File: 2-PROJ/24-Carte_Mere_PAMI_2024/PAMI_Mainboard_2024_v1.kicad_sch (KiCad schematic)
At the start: 20 parts, among them J1 Conn_01x08, J2 Conn_01x03, J3 USB_A, J4 Conn_01x03, J5 Conn_01x02, J6 Conn_01x04, J7 Conn_01x03, SW1 SW_DIP_x04, SW2 SW_DPST_x2

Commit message: Carte Mère PAMI - Work In Progress
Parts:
- added J24: Conn_01x06, Connector_PinSocket_2.54mm:PinSocket_1x06_P2.54mm_Vertical, symbol Connector_Generic:Conn_01x06
- added J25: Conn_02x05_Odd_Even, ConnectorsEvo:690357281076, symbol Connector_Generic:Conn_02x05_Odd_Even
- SW2: footprint (none) -> Connector_PinHeader_2.54mm:PinHeader_1x03_P2.54mm_Vertical
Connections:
- net +3.3VP: now also J24.3 (Pin_3)
- net +5V: now also J7.2 (Pin_2), J24.1 (Pin_1), J25.1 (Pin_1); no longer J7.1 (Pin_1)
- net CAN/CANH: now also J25.9 (Pin_9)
- net CAN/CANL: now also J25.10 (Pin_10)
- net CaptTOR_1: now also RP1.26 (GPIO7/SPI0_CE1)
- net CaptTOR_2: now also RP1.29 (GPIO5/GPCLK1)
- net GND: now also J7.1 (Pin_1), J24.2 (Pin_2), J24.6 (Pin_6), J25.3 (Pin_3), J25.4 (Pin_4); no longer J7.2 (Pin_2)
- net SIDE: now also RP1.18 (GPIO24)
- net at R9.1: now also RP1.7 (GPIO4/GPCLK0), SW1.4; no longer SW1.1
- net at R11.1: now also RP1.16 (GPIO23), SW1.2; no longer SW1.3
- net +5V_IN: now reaches J1.8 (Pin_8), SW2.2 (B)
- net at R10.1: now also RP1.13 (GPIO27), SW1.3; no longer SW1.2
- net at R12.1: now also RP1.15 (GPIO22), SW1.1; no longer SW1.4
- net at RP1.10 (GPIO15/UART_RX): now also J24.4 (Pin_4)
- net at RP1.8 (GPIO14/UART_TX): now also J24.5 (Pin_5)
- net CAN/INT renamed INT_CAN
- net SX1509/INT renamed INT_SX
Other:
- note added: "JeVois A33 alim & UART"
- note added: "Movement Tracker"
- moved on the sheet: J5, J7

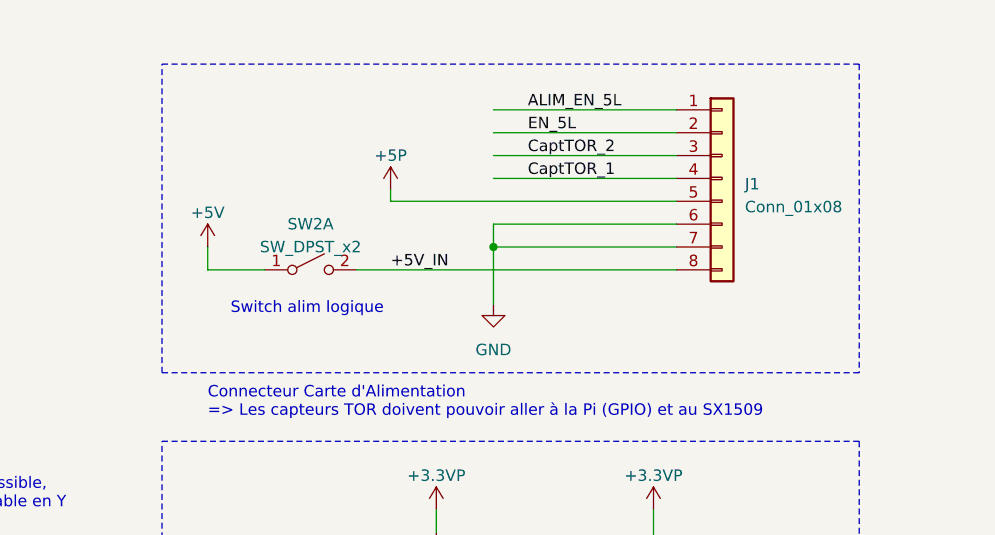
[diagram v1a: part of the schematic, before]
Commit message: CM PAMI 2024 - Correction interrupteur 5V
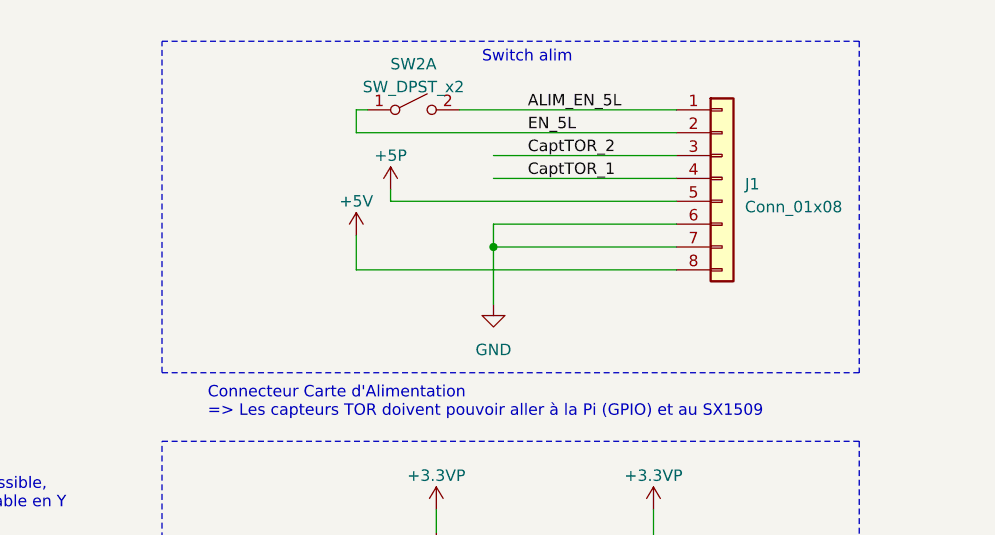
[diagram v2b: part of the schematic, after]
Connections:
- net +5V: now also J1.8 (Pin_8); no longer SW2.1 (A)
- net ALIM_EN_5L: now also SW2.2 (B)
- net EN_5L: now also SW2.1 (A)
- removed net +5V_IN: J1.8 (Pin_8), SW2.2 (B)
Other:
- note added: "Switch alim"
- note removed: "Switch alim logique"
- moved on the sheet: SW2A
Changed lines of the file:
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@@
+    (stroke (width 0) (type default))
+  )
+  (wire (pts (xy 220.98 24.13) (xy 219.71 24.13))
     (stroke (width 0) (type default))
   )
@@
     (stroke (width 0) (type default))
   )
-  (wire (pts (xy 234.95 24.13) (xy 255.27 24.13))
+  (wire (pts (xy 231.14 24.13) (xy 255.27 24.13))
     (stroke (width 0) (type default))
   )
@@
     (stroke (width 0) (type default))
   )
+  (wire (pts (xy 219.71 38.1) (xy 219.71 41.91))
+    (stroke (width 0) (type default))
+  )
   (wire (pts (xy 67.31 86.36) (xy 160.02 86.36))
     (stroke (width 0) (type default))
@@
     (stroke (width 0) (type default))
   )
-  (wire (pts (xy 209.55 41.91) (xy 203.2 41.91))
-    (stroke (width 0) (type default))
-  )
   (wire (pts (xy 67.31 53.34) (xy 71.12 53.34))
     (stroke (width 0) (type default))
@@
     (stroke (width 0) (type default))
   )
-  (wire (pts (xy 203.2 41.91) (xy 203.2 39.37))
-    (stroke (width 0) (type default))
-  )
   (wire (pts (xy 267.97 133.35) (xy 267.97 135.89))
     (stroke (width 0) (type default))
@@
     (stroke (width 0) (type default))
   )
+  (wire (pts (xy 255.27 41.91) (xy 219.71 41.91))
+    (stroke (width 0) (type default))
+  )
   (wire (pts (xy 83.82 38.1) (xy 82.55 38.1))
     (stroke (width 0) (type default))
@@
     (stroke (width 0) (type default))
   )
-  (wire (pts (xy 234.95 26.67) (xy 255.27 26.67))
+  (wire (pts (xy 219.71 26.67) (xy 255.27 26.67))
     (stroke (width 0) (type default))
   )
@@
     (stroke (width 0) (type default))
   )
+  (wire (pts (xy 219.71 24.13) (xy 219.71 26.67))
+    (stroke (width 0) (type default))
+  )
   (wire (pts (xy 68.58 162.56) (xy 68.58 165.1))
     (stroke (width 0) (type default))
@@
   )
   (wire (pts (xy 67.31 74.93) (xy 86.36 74.93))
-    (stroke (width 0) (type default))
-  )
-  (wire (pts (xy 255.27 41.91) (xy 219.71 41.91))
     (stroke (width 0) (type default))
   )
@@
     (fill (type none))
   )
-  (rectangle (start 198.12 19.05) (end 275.59 53.34)
+  (rectangle (start 198.12 16.51) (end 275.59 53.34)
     (stroke (width 0) (type dash))
     (fill (type none))
@@
     (effects (font (size 1.27 1.27)) (justify left bottom))
   )
-  (text "Switch alim logique" (at 205.74 46.99 0)
+  (text "Switch alim" (at 233.68 19.05 0)
     (effects (font (size 1.27 1.27)) (justify left bottom))
   )
@@
   )
   (label "SIDE" (at 208.28 151.13 0) (fields_autoplaced)
-    (effects (font (size 1.27 1.27)) (justify left bottom))
-  )
-  (label "+5V_IN" (at 223.52 41.91 0) (fields_autoplaced)
     (effects (font (size 1.27 1.27)) (justify left bottom))
   )
@@
     )
   )
-  (symbol (lib_id "Switch:SW_DPST_x2") (at 214.63 41.91 0) (unit 1)
-    (in_bom yes) (on_board yes) (dnp no) (fields_autoplaced)
-    (property "Reference" "SW2" (at 214.63 36.83 0)
-      (effects (font (size 1.27 1.27)))
-    )
-    (property "Value" "SW_DPST_x2" (at 214.63 39.37 0)
-      (effects (font (size 1.27 1.27)))
-    )
-    (property "Footprint" "Connector_PinHeader_2.54mm:PinHeader_1x03_P2.54mm_Vertical" (at 214.63 41.91 0)
-      (effects (font (size 1.27 1.27)) hide)
-    )
-    (property "Datasheet" "~" (at 214.63 41.91 0)
+  (symbol (lib_id "Switch:SW_DPST_x2") (at 226.06 24.13 0) (unit 1)
+    (in_bom yes) (on_board yes) (dnp no) (fields_autoplaced)
+    (property "Reference" "SW2" (at 226.06 19.05 0)
+      (effects (font (size 1.27 1.27)))
+    )
+    (property "Value" "SW_DPST_x2" (at 226.06 21.59 0)
+      (effects (font (size 1.27 1.27)))
+    )
+    (property "Footprint" "Connector_PinHeader_2.54mm:PinHeader_1x03_P2.54mm_Vertical" (at 226.06 24.13 0)
+      (effects (font (size 1.27 1.27)) hide)
+    )
+    (property "Datasheet" "~" (at 226.06 24.13 0)
       (effects (font (size 1.27 1.27)) hide)
     )
@@
     )
   )
-  (symbol (lib_id "power:+5V") (at 203.2 39.37 0) (unit 1)
-    (in_bom yes) (on_board yes) (dnp no) (fields_autoplaced)
-    (property "Reference" "#PWR021" (at 203.2 43.18 0)
-      (effects (font (size 1.27 1.27)) hide)
-    )
-    (property "Value" "+5V" (at 203.2 35.56 0)
-      (effects (font (size 1.27 1.27)))
-    )
-    (property "Footprint" "" (at 203.2 39.37 0)
-      (effects (font (size 1.27 1.27)) hide)
-    )
-    (property "Datasheet" "" (at 203.2 39.37 0)
-      (effects (font (size 1.27 1.27)) hide)
-    )
+  (symbol (lib_id "power:+5V") (at 219.71 38.1 0) (unit 1)
+    (in_bom yes) (on_board yes) (dnp no) (fields_autoplaced)
+    (property "Reference" "#PWR021" (at 219.71 41.91 0)
+      (effects (font (size 1.27 1.27)) hide)
+    )
+    (property "Value" "+5V" (at 219.71 34.29 0)
+      (effects (font (size 1.27 1.27)))
+    )
+    (property "Footprint" "" (at 219.71 38.1 0)
+      (effects (font (size 1.27 1.27)) hide)
+    )
+    (property "Datasheet" "" (at 219.71 38.1 0)
+      (effects (font (size 1.27 1.27)) hide)
+    )

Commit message: CM PAMI 2024 - WIP
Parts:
- added C11: 100nF, Capacitor_SMD:C_0603_1608Metric, symbol Device:C
- added C8: 470uF, Capacitor_THT:C_Radial_D8.0mm_H11.5mm_P3.50mm, symbol Device:C_Polarized_Small
- added D1: LED, LED_SMD:LED_0603_1608Metric, symbol Device:LED
- added H1, H2, H3, H4: MountingHole_Pad, MountingHole:MountingHole_3.2mm_M3_Pad_Via, symbol Mechanical:MountingHole_Pad
- added R16, R17, R18, R19, R22: 10K, Resistor_SMD:R_0603_1608Metric_Pad0.98x0.95mm_HandSolder, symbol Device:R
- added R20: 68, Resistor_SMD:R_0603_1608Metric_Pad0.98x0.95mm_HandSolder, symbol Device:R
- added R21: R, Resistor_SMD:R_0603_1608Metric, symbol Device:R
- added R23, R24, R25, R26: 1K, Resistor_SMD:R_0603_1608Metric_Pad0.98x0.95mm_HandSolder, symbol Device:R
- R13: value 68 -> 1K
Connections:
- net +3.3VP: now also C11.1, R22.2; no longer J4.1 (Pin_1), RP1.1 (3V3)
- net +5P: now also D1.2 (A)
- net +5V: now also C8.1
- net CaptTOR_1: now also R18.2
- net CaptTOR_2: now also R16.2
- net GND: now also C11.2, C8.2, H1.1, H2.1, H3.1, H4.1, R17.1, R19.1, R21.1
- net WS2812B: now also R20.2; no longer J7.3 (Pin_3)
- net at R9.1, SW1.4: now also R26.1; no longer RP1.7 (GPIO4/GPCLK0)
- net at R11.1, SW1.2: now also R24.1; no longer RP1.16 (GPIO23)
- net at R12.1, SW1.1: now also R23.1; no longer RP1.15 (GPIO22)
- net at R10.1, SW1.3: now also R25.1; no longer RP1.13 (GPIO27)
- net at J4.2 (Pin_2), R13.1: now also R22.1
- new net: R16.1, R17.2
- new net: R23.2, RP1.15 (GPIO22)
- new net: J7.3 (Pin_3), R20.1
- new net: R18.1, R19.2
- new net: D1.1 (K), R21.2
- new net: R25.2, RP1.13 (GPIO27)
- new net: R26.2, RP1.7 (GPIO4/GPCLK0)
- new net: R24.2, RP1.16 (GPIO23)
- no-connect marks 0 -> 1
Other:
- note added: "Raccorder I2C du movement tracker"
- note added: "Raccorder le reset du tracker à une GPIO de la Pi Rajouter un bouton de "reset sauf Raspi""
- note added: "Trouver modele 3D pour le switch"
- note removed: "Vers 5 GPIO Raspi"
- moved on the sheet: C14, C15, J2, J24, R13, R7, R8

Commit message: CM PAMI 2024 - WIP
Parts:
- added D2, D3, D4: WS2812B, LED_SMD:LED_WS2812B_PLCC4_5.0x5.0mm_P3.2mm, symbol LED:WS2812B
- R21: value R -> 1K
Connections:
- net +5V: now also D2.1 (VDD), D3.1 (VDD), D4.1 (VDD)
- net GND: now also D2.3 (VSS), D3.3 (VSS), D4.3 (VSS)
- net at J7.3 (Pin_3): now also D4.2 (DOUT); no longer R20.1
- new net: D3.2 (DOUT), D4.4 (DIN)
- new net: D2.2 (DOUT), D3.4 (DIN)
- new net: D2.4 (DIN), R20.1
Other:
- moved on the sheet: J7

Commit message: fin routage carte Mere PAMI
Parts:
- added R43: 68, Resistor_SMD:R_0603_1608Metric_Pad0.98x0.95mm_HandSolder, symbol Device:R
- J24: footprint Connector_PinSocket_2.54mm:PinSocket_1x06_P2.54mm_Vertical -> Connector_PinHeader_2.54mm:PinHeader_1x06_P2.54mm_Vertical
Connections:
- net SX1509/SCL: now also J25.6 (Pin_6)
- net SX1509/SDA: now also J25.5 (Pin_5)
- net at J25.7 (Pin_7): now also R43.1
- net MouvT_INT: now reaches RP1.38 (GPIO20/SPI1_MOSI)
- net MouvT_INT: now also R43.2
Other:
- moved on the sheet: J6

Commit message: correction de l'empreinte du mouvement tracker (690357281076 au lieu de 690367281076)
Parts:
- J25: footprint ConnectorsEvo:690357281076 -> ConnectorsEvo:690367281076
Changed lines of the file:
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@@
       (effects (font (size 1.27 1.27)))
     )
-    (property "Footprint" "ConnectorsEvo:690357281076" (at 160.02 38.1 0)
+    (property "Footprint" "ConnectorsEvo:690367281076" (at 160.02 38.1 0)
       (effects (font (size 1.27 1.27)) hide)
     )

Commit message: CM PAMI 2024 - Propretés sur le schéma
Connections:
- net SX1509/SCL renamed SCL1
- net SX1509/SDA renamed SDA1
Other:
- note added: "Connecteur Carte d'Alimentation"
- note removed: "Connecteur Carte d'Alimentation => Les capteurs TOR doivent pouvoir aller à la Pi (GPIO) et au SX1509"
- note removed: "L'OLED dispose d'un LDO: Il peut être alimenté en 5V"
- note removed: "Plusieurs prises CAN sont possible, ou bien une seule avec un cable en Y"
- note removed: "Prévoir connecteur pour LED RGB sérielles type WS2812B: - Alim 5V, GND, 1 pin de contrôle sur Raspi (GPIO type PWM obligatoire) Prise pour le "movement tracker" Prises JeVois (header unique power 5V + UART)"
- note removed: "Raccorder I2C du movement tracker"
- note removed: "Raccorder le reset du tracker à une GPIO de la Pi Rajouter un bouton de "reset sauf Raspi""
- note removed: "Trouver modele 3D pour le switch"
- moved on the sheet: D2, D3, D4, H1, H2, H3, H4, J5, J7, R10, R11, R12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
